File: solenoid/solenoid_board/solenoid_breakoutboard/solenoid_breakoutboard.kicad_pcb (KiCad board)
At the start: 2 copper layers, 15.5 x 23 mm, 8 parts, among them Q1 AO4842, U1 PCA9536DP

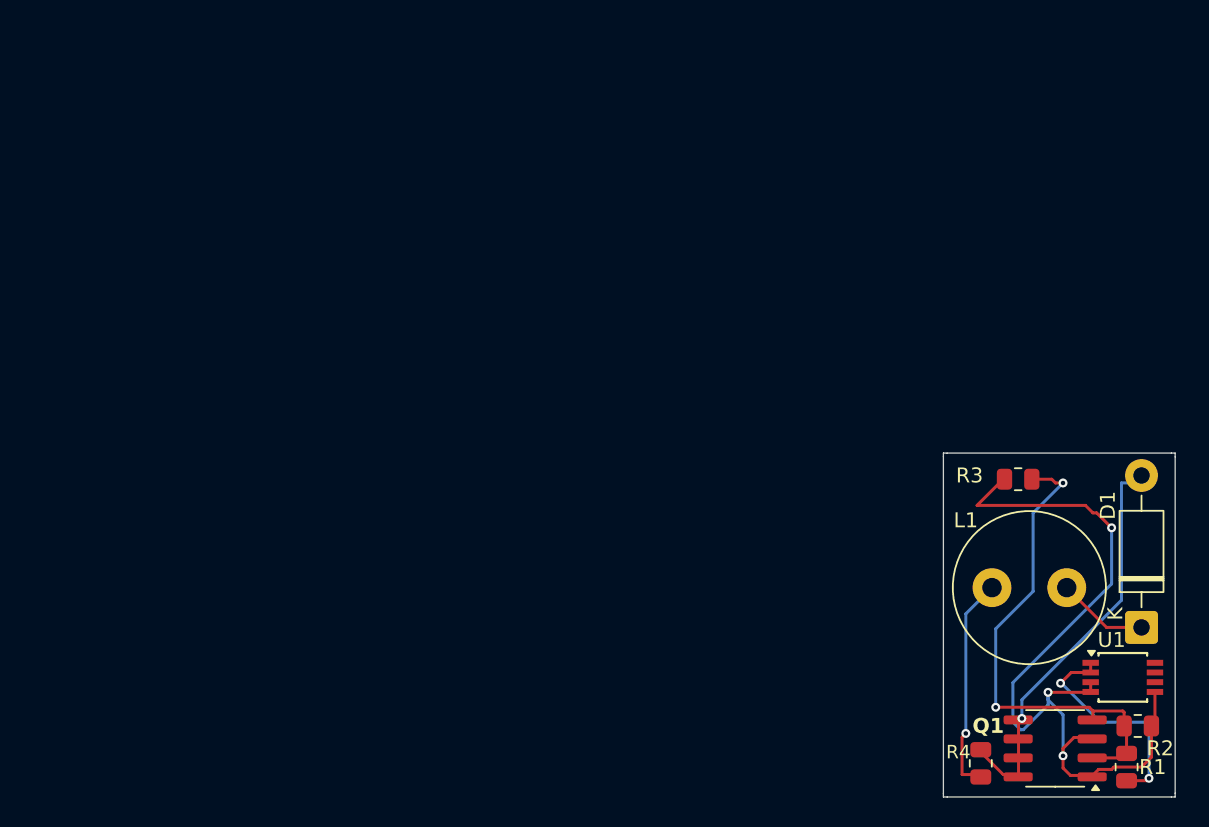
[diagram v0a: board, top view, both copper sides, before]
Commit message: finished solenoid breakout schematic + started on PCB
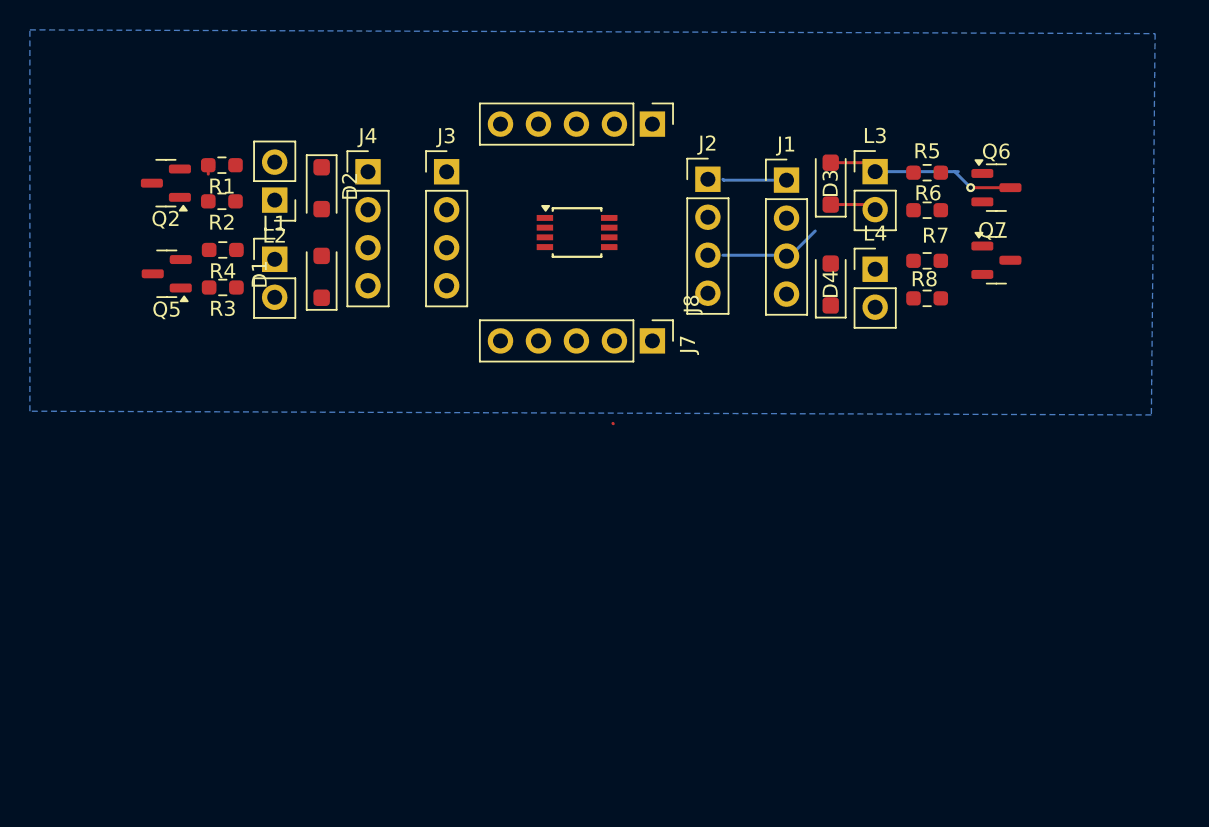
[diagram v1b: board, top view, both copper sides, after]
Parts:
- removed Q1: AO4842, Package_SO:SOIC-8_3.9x4.9mm_P1.27mm
- added D2: 1N4001, Diode_SMD:D_SOD-123F, F.Cu at (73.2, 56.0)
- added D3: 1N4001, Diode_SMD:D_SOD-123F, F.Cu at (107.2, 55.7)
- added D4: 1N4001, Diode_SMD:D_SOD-123F, F.Cu at (107.2, 62.5)
- added J1: Conn_01x04_Pin, Connector_PinHeader_2.54mm:PinHeader_1x04_P2.54mm_Vertical, F.Cu at (104.3, 55.5)
- added J2: Conn_01x04_Pin, Connector_PinHeader_2.54mm:PinHeader_1x04_P2.54mm_Vertical, F.Cu at (99.0, 55.4)
- added J3: Conn_01x04_Pin, Connector_PinHeader_2.54mm:PinHeader_1x04_P2.54mm_Vertical, F.Cu at (81.5, 54.9)
- added J4: Conn_01x04_Pin, Connector_PinHeader_2.54mm:PinHeader_1x04_P2.54mm_Vertical, F.Cu at (76.3, 54.9)
- added J7: Conn_01x05, Connector_PinHeader_2.54mm:PinHeader_1x05_P2.54mm_Vertical, F.Cu at (95.3, 66.2)
- added J8: Conn_01x05, Connector_PinHeader_2.54mm:PinHeader_1x05_P2.54mm_Vertical, F.Cu at (95.3, 51.8)
- added L2: L, Connector_PinHeader_2.54mm:PinHeader_1x02_P2.54mm_Vertical, F.Cu at (70.0, 56.8)
- added L3: L, Connector_PinHeader_2.54mm:PinHeader_1x02_P2.54mm_Vertical, F.Cu at (110.2, 54.9)
- added L4: L, Connector_PinHeader_2.54mm:PinHeader_1x02_P2.54mm_Vertical, F.Cu at (110.2, 61.5)
- added Q2: AO3400A, Package_TO_SOT_SMD:SOT-23, F.Cu at (62.8, 55.7)
- added Q5: AO3400A, Package_TO_SOT_SMD:SOT-23, F.Cu at (62.8, 61.8)
- added Q6: AO3400A, Package_TO_SOT_SMD:SOT-23, F.Cu at (118.3, 56.0)
- added Q7: AO3400A, Package_TO_SOT_SMD:SOT-23, F.Cu at (118.3, 60.9)
- added R5: 500, Resistor_SMD:R_0603_1608Metric_Pad0.98x0.95mm_HandSolder, F.Cu at (113.7, 55.0)
- added R6: 10K, Resistor_SMD:R_0603_1608Metric_Pad0.98x0.95mm_HandSolder, F.Cu at (113.7, 57.5)
- added R7: 500, Resistor_SMD:R_0603_1608Metric_Pad0.98x0.95mm_HandSolder, F.Cu at (113.7, 60.9)
- added R8: 10K, Resistor_SMD:R_0603_1608Metric_Pad0.98x0.95mm_HandSolder, F.Cu at (113.7, 63.4)
- D1: footprint Diode_THT:D_DO-41_SOD81_P10.16mm_Horizontal -> Diode_SMD:D_SOD-123F
- L1: footprint Inductor_THT:L_Radial_D10.0mm_P5.00mm_Fastron_07M -> Connector_PinHeader_2.54mm:PinHeader_1x02_P2.54mm_Vertical
- R1: value 100K -> 500; footprint Resistor_SMD:R_0805_2012Metric -> Resistor_SMD:R_0603_1608Metric_Pad0.98x0.95mm_HandSolder
- R2: footprint Resistor_SMD:R_0805_2012Metric -> Resistor_SMD:R_0603_1608Metric_Pad0.98x0.95mm_HandSolder
- R3: value 1.8K -> 500; footprint Resistor_SMD:R_0805_2012Metric -> Resistor_SMD:R_0603_1608Metric_Pad0.98x0.95mm_HandSolder
- R4: value R -> 10K; footprint Resistor_SMD:R_0805_2012Metric -> Resistor_SMD:R_0603_1608Metric_Pad0.98x0.95mm_HandSolder
- moved R1 72.7 mm to (66.5, 54.5), turned to 180 degrees
- moved R2 70.6 mm to (66.5, 56.9), turned to 180 degrees
- moved R4 61.2 mm to (66.6, 60.2), turned to 180 degrees
- moved D1 59.6 mm to (73.2, 62.0)
- moved R3 54.7 mm to (66.6, 62.7)
- moved L1 52.8 mm to (70.0, 60.8)
- moved U1 47.1 mm to (90.2, 59.0)
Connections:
- L1 pad 1: Net-(L1-Pad1) -> Net-(D1-A)
- R1 pad 1: Net-(U1-IO0) -> Net-(J3-Pin_2)
- R1 pad 2: Net-(Q1A-G1) -> Net-(Q5-G)
- R2 pad 1: Net-(Q1A-G1) -> Net-(Q5-G)
- R3 pad 1: Net-(Q1A-G1) -> Net-(J4-Pin_2)
- R3 pad 2: GND -> Net-(Q2-G)
- R4 pad 1: Net-(D1-A) -> Net-(Q2-G)
- R4 pad 2: Net-(L1-Pad1) -> GND
- U1 pad 1: Net-(U1-IO0) -> Net-(J3-Pin_2)
- U1 pad 2: Net-(U1-IO0) -> Net-(J4-Pin_2)
- U1 pad 3: GND -> Net-(J2-Pin_2)
- U1 pad 5: GND -> Net-(J1-Pin_2)
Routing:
- net GND: track 54.9 -> 1.03 mm, vias 3 -> 0
- net Net-(Q1A-G1): track 34.0 -> 0.00 mm, vias 2 -> 0
- net Net-(D1-A): track 27.3 -> 0.00 mm, vias 1 -> 0
- net Net-(U1-IO0): track 15.4 -> 0.00 mm, vias 2 -> 0
- net Net-(L1-Pad1): track 14.4 -> 0.00 mm, vias 1 -> 0
- net Net-(D3-A): track 0.00 -> 13.0 mm, vias 0 -> 1
- net +3.3V: track 0.00 -> 4.52 mm
- net Net-(D3-K): track 0.00 -> 3.11 mm
- net +5V: track 6.10 -> 6.99 mm
- added copper zone on B.Cu, net (none)
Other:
- board outline removed
- board text removed: "Lakshay Yadav"
